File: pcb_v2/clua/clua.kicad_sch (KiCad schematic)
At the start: 168 parts, among them J1 bus_ula_2, J10 bus_rf16_3, J11 UCODE_1, J12 UCODE_2, J13 UCODE_3, J14 UCODE_4, J15 UCODE_5, J16 UCODE_6, J17 UCODE_7, J18 UCODE_INT, J19 9V 1A, J2 bus_ula_1, J20 VOLTMETER, J21 AMPMETER, J3 bus_rf16_1, J4 bus_rf16_2, J5 bus mem 1, J6 bus mem 2, J7 UCODE_0, J8 bus_mgrf_1, J9 bus_mgrf_2, Q1 BC548, Q2 BC548, SW1 RESET, U1 74LS193, U10 MC14495P, U11 IR_HIGH, U12 74LS574, U13 MC14495P, U14 RDADDR_LOW, U15 74LS04, U16 74LS86, U17 RDADDR_HIGH, U18 74LS244, U19 74LS04, U2 74HC238, U20 74LS08, U21 MC14495P, U22 WRADDR_HIGH, U23 WRADDR_LOW, U24 74LS86, U25 74LS125, U26 74LS32, U27 74LS08, U28 74LS74, U29 74LS74, U3 74LS32, U30 74LS138, U31 MC14495P, U32 74HC238, U33 74LS32, U34 LM7805, U4 74LS04, U5 74LS08, U6 74LS157, U7 74LS157, U8 74LS574, U9 IR_LOW

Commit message: .
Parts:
- removed C11: 0.33uF, Capacitor_THT:CP_Radial_D5.0mm_P2.50mm, symbol Device:C_Polarized
- removed C13, C15, C21, C25 (x2), C3, C5: 100nF, Capacitor_THT:C_Disc_D5.1mm_W3.2mm_P5.00mm, symbol Device:C
- removed C14: 0.1uF, Capacitor_THT:CP_Radial_D5.0mm_P2.50mm, symbol Device:C_Polarized
- removed D25, D27, D28, D29, D31: 1N4148, Diode_THT:D_DO-35_SOD27_P7.62mm_Horizontal, symbol Diode:1N4148
- removed D32: 1N4001, Diode_THT:D_DO-41_SOD81_P10.16mm_Horizontal, symbol Diode:1N4001
- removed J10: bus_rf16_3, Connector_PinHeader_2.54mm:PinHeader_2x08_P2.54mm_Vertical, symbol Connector_Generic:Conn_02x08_Odd_Even
- removed J19: 9V 1A, symbol Connector_Generic:Conn_01x02
- removed J20: VOLTMETER, symbol Connector_Generic:Conn_01x02
- removed J21: AMPMETER, symbol Connector_Generic:Conn_01x02
- removed J4: bus_rf16_2, Connector_PinHeader_2.54mm:PinHeader_2x08_P2.54mm_Vertical, symbol Connector_Generic:Conn_02x08_Odd_Even
- removed J5: bus mem 1, Connector_PinHeader_2.54mm:PinHeader_2x08_P2.54mm_Vertical, symbol Connector_Generic:Conn_02x08_Odd_Even
- removed J6: bus mem 2, Connector_PinHeader_2.54mm:PinHeader_2x08_P2.54mm_Vertical, symbol Connector_Generic:Conn_02x08_Odd_Even
- removed J8: bus_mgrf_1, Connector_PinHeader_2.54mm:PinHeader_2x08_P2.54mm_Vertical, symbol Connector_Generic:Conn_02x08_Odd_Even
- removed J9: bus_mgrf_2, Connector_PinHeader_2.54mm:PinHeader_2x08_P2.54mm_Vertical, symbol Connector_Generic:Conn_02x08_Odd_Even
- removed Q1, Q2: BC548, Package_TO_SOT_THT:TO-92_Inline, symbol Transistor_BJT:BC548
- removed R10, R11, R15, R16, R17, R18, R19, R36, R37, R38, R39, R40, R41, R42, R43, R44, R45, R46, R47, R48, R49, R50, R51, R52, R7, R8, R9: 10K, symbol Device:R
- removed R12, R20: 470R, symbol Device:R
- removed R21, R22: 10K, Resistor_THT:R_Axial_DIN0207_L6.3mm_D2.5mm_P7.62mm_Horizontal, symbol Device:R
- removed U13, U21: MC14495P, Package_DIP:DIP-16_W7.62mm, symbol Driver_LED:MC14495P
- removed U14: RDADDR_LOW, 7segdisplay:1-digit-13mm, symbol Display_Character:SA39-11EWA
- removed U15: 74LS04, symbol 74xx:74LS04
- removed U17: RDADDR_HIGH, 7segdisplay:1-digit-13mm, symbol Display_Character:SA39-11EWA
- removed unit 4 of U19
- removed U22: WRADDR_HIGH, 7segdisplay:1-digit-13mm, symbol Display_Character:SA39-11EWA
- removed U23: WRADDR_LOW, 7segdisplay:1-digit-13mm, symbol Display_Character:SA39-11EWA
- removed U3, U33: 74LS32, symbol 74xx:74LS32
- removed U34: LM7805, Package_TO_SOT_THT:TO-220-3_Vertical, symbol Regulator_Linear:LM7805_TO220
- removed unit 7 of U4
- removed unit 5 of U4
- removed unit 2 of U4
- removed unit 1 of U4
- removed unit 3 of U5
- removed unit 5 of U5
- removed unit 2 of U5
- added C24, C25: 100nF, Capacitor_THT:C_Disc_D5.1mm_W3.2mm_P5.00mm, symbol Device:C
- added R2: 10K, symbol Device:R
- added unit 3 of U16
- added unit 2 of U16
- added unit 4 of U16
- added unit 6 of U19
- added unit 3 of U19
- added unit 3 of U27
- added U4: 74LS02, symbol 74xx:74LS02
- J1: value bus_ula_2 -> bus clu 1
- J2: value bus_ula_1 -> bus clu 2
- J3: value bus_rf16_1 -> bus clu 3
- renumbered U4 to U19, U27 to U20, U5 to U27
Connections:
- net UC_read_mem_pc is gone; now on net fetch_cycle: D10.2 (A), D11.2 (A), D12.2 (A), D8.2 (A), D9.2 (A)
- net ~{UC_int_cycle} is gone; now on net ~{UC_int_ready}: R24.1
- net ~{UC_rd_addr_src_reg} is gone; now on net ~{UC_read_addr_src_reg}: U12.1 (OE)
- net ~{clock} is gone; now on net CLOCK: U1.5 (UP)
- net +5V: now also J1.1 (Pin_1), J1.2 (Pin_2), U25.10, U25.12, U25.13, U25.9, C24.2, C25.2, R2.2, U16.10, U16.12, U16.4, U16.5, U16.9, U4.14 (VCC); no longer J2.1 (Pin_1), J2.2 (Pin_2), J3.1 (Pin_1), J3.2 (Pin_2)
- net ADDR_{0}: now also J3.2 (Pin_2)
- net ADDR_{1}: now also J3.1 (Pin_1)
- net CARRY_FLAG: now also J3.6 (Pin_6); no longer J2.8 (Pin_8)
- net CLOCK: now also J2.15 (Pin_15), U27.9; no longer J1.4 (Pin_4)
- net DATA_{0}: now also J1.14 (Pin_14); no longer J2.14 (Pin_14), J3.14 (Pin_14)
- net DATA_{1}: now also J1.13 (Pin_13); no longer J2.13 (Pin_13), J3.13 (Pin_13)
- net DATA_{2}: now also J1.11 (Pin_11); no longer J2.11 (Pin_11), J3.11 (Pin_11)
- net DATA_{3}: now also J1.9 (Pin_9); no longer J2.9 (Pin_9), J3.9 (Pin_9)
- net DATA_{4}: now also J1.7 (Pin_7); no longer J2.7 (Pin_7), J3.7 (Pin_7)
- net DATA_{5}: now also J1.5 (Pin_5); no longer J2.5 (Pin_5), J3.5 (Pin_5)
- net DATA_{6}: now also J1.3 (Pin_3); no longer J2.3 (Pin_3), J3.3 (Pin_3)
- net DATA_{7}: now also J1.4 (Pin_4); no longer J2.4 (Pin_4), J3.4 (Pin_4)
- net GND: now also J1.15 (Pin_15), J1.16 (Pin_16), C24.1, C25.1, U4.7 (GND); no longer J2.15 (Pin_15), J2.16 (Pin_16), J3.15 (Pin_15), J3.16 (Pin_16)
- net INT_MASK_FLAG: now also J3.12 (Pin_12); no longer J1.1 (Pin_1)
- net INT_REQUEST: now also J2.2 (Pin_2)
- net NEGATIVE_FLAG: now also J3.10 (Pin_10); no longer J2.12 (Pin_12)
- net OVERFLOW_FLAG: now also J3.8 (Pin_8); no longer J2.10 (Pin_10)
- net RD_ADDR_0: now also J2.8 (Pin_8); no longer J1.8 (Pin_8)
- net RD_ADDR_1: now also J2.10 (Pin_10); no longer J1.10 (Pin_10)
- net RD_ADDR_2: now also J2.12 (Pin_12); no longer J1.12 (Pin_12)
- net RD_ADDR_3: now also J2.14 (Pin_14); no longer J1.14 (Pin_14)
- net RD_ADDR_4: now also J2.16 (Pin_16); no longer J1.16 (Pin_16)
- net RESET: now also U4.12
- net UC_const_boot_addr: now also U19.6
- net UC_read_mem_const: no longer D26.1 (K)
- net ULA_ENABLE: now also J2.4 (Pin_4), U16.11; no longer J1.2 (Pin_2)
- net WRITE_ENABLE: now also J2.6 (Pin_6), U4.10; no longer J1.15 (Pin_15)
- net WR_ADDR_0: now also J2.5 (Pin_5); no longer J1.5 (Pin_5)
- net WR_ADDR_1: now also J2.7 (Pin_7); no longer J1.7 (Pin_7)
- net WR_ADDR_2: now also J2.9 (Pin_9); no longer J1.9 (Pin_9)
- net WR_ADDR_3: now also J2.11 (Pin_11); no longer J1.11 (Pin_11)
- net WR_ADDR_4: now also J2.13 (Pin_13); no longer J1.13 (Pin_13)
- net ZERO_FLAG: now also J3.4 (Pin_4); no longer J2.6 (Pin_6)
- net fetch_cycle: now also U27.10; no longer J11.16 (Pin_16), J12.16 (Pin_16), J13.16 (Pin_16), J14.16 (Pin_16), J15.16 (Pin_16), J16.16 (Pin_16), J17.16 (Pin_16), J18.16 (Pin_16), J7.16 (Pin_16)
- net low_cycle: now also U4.6
- net reset_high_cycle: now also U4.3
- net reset_low_cycle: now also U4.2, U4.5; no longer D26.2 (A), D30.2 (A)
- net ~{UC_break}: now also J3.5 (Pin_5)
- net ~{UC_int_ready}: now also U19.9; no longer U19.13
- net ~{UC_pcia_swap}: now also J2.3 (Pin_3)
- net ~{UC_pclr_swap}: now also J2.1 (Pin_1)
- net ~{UC_read_mem_const}: now also D26.2 (A), R2.1
- net ~{UC_restart_cycle}: now also D23.2 (A), U1.11 (~{LOAD})
- net ~{UC_ula_enable}: now also U16.13
- net ~{UC_write_enable}: now also D30.2 (A), U4.8
- net ~{condition_true}: now also U4.9
- net at U2.9 (Y6): now also U19.13; no longer D23.2 (A)
- net fetch_clock: now reaches U8.11 (Cp)
- net fetch_clock: now also J11.16 (Pin_16), J12.16 (Pin_16), J13.16 (Pin_16), J14.16 (Pin_16), J15.16 (Pin_16), J16.16 (Pin_16), J17.16 (Pin_16), J18.16 (Pin_16), J7.16 (Pin_16), U27.8
- net at U28.11 (C): now also U19.8; no longer U19.12
- net at U25.2: now also U4.4
- net at U19.4: now also U4.11
- net at U28.1 (~{R}): now also U4.13
- net UC_restart_cycle: no longer names the net of D23.1 (K)
- net UC_restart_cycle: now also U19.12
- net UC_write_enable: no longer names the net of D30.1 (K)
- net UC_write_enable: now also D26.1 (K), U19.5, U4.1
- net condition_true: no longer names the net of U28.6 (~{Q})
- no-connect marks 136 -> 120
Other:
- moved on the sheet: C12, C18, D10, D11, D12, D13, D14, D15, D16, D17, D18, D19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

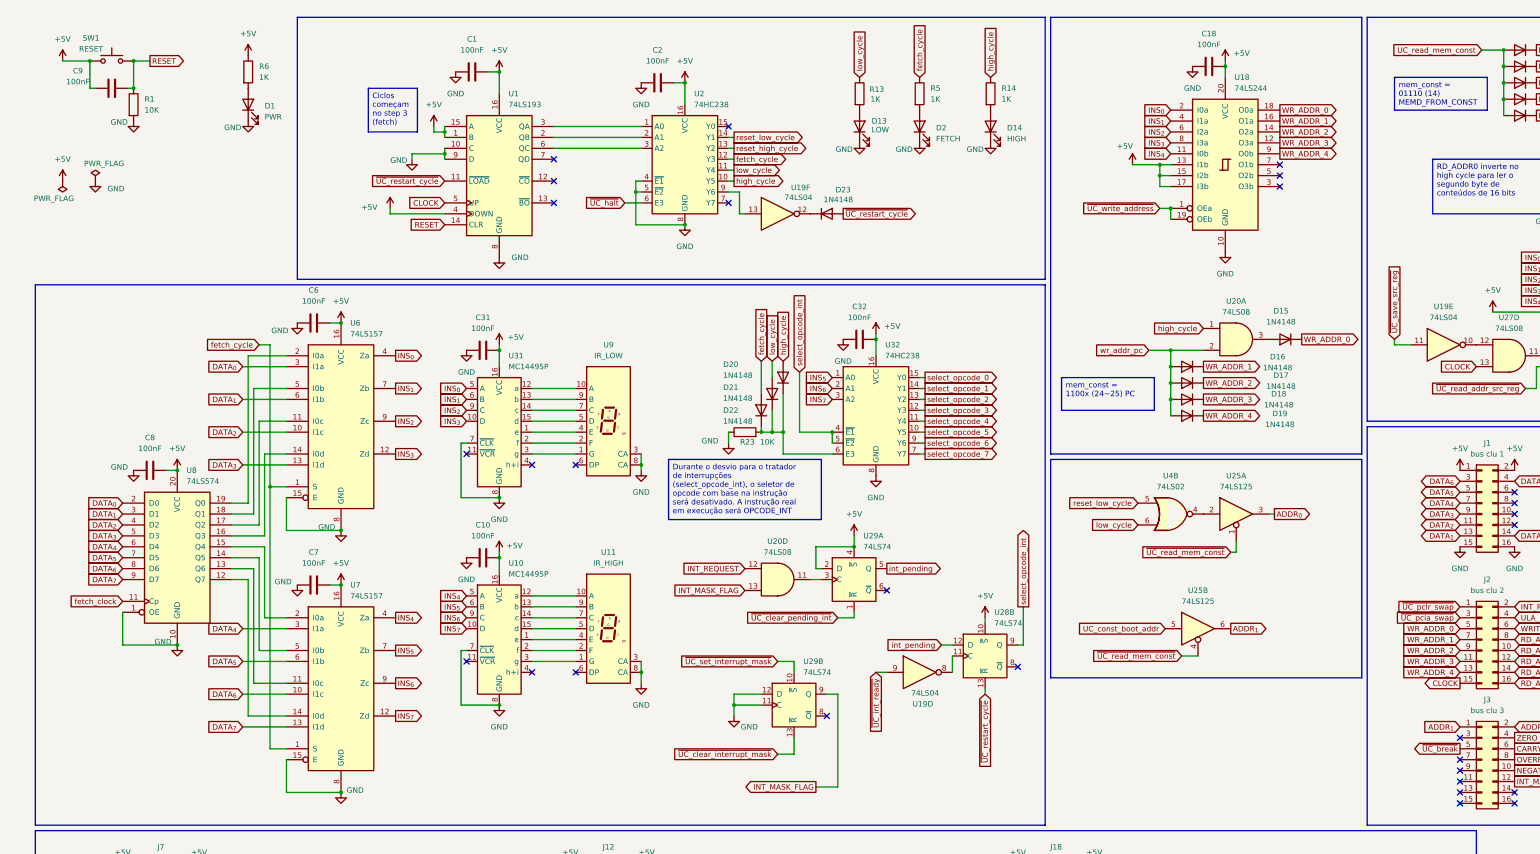
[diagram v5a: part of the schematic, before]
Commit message: movendo itens da clu para o sysbus
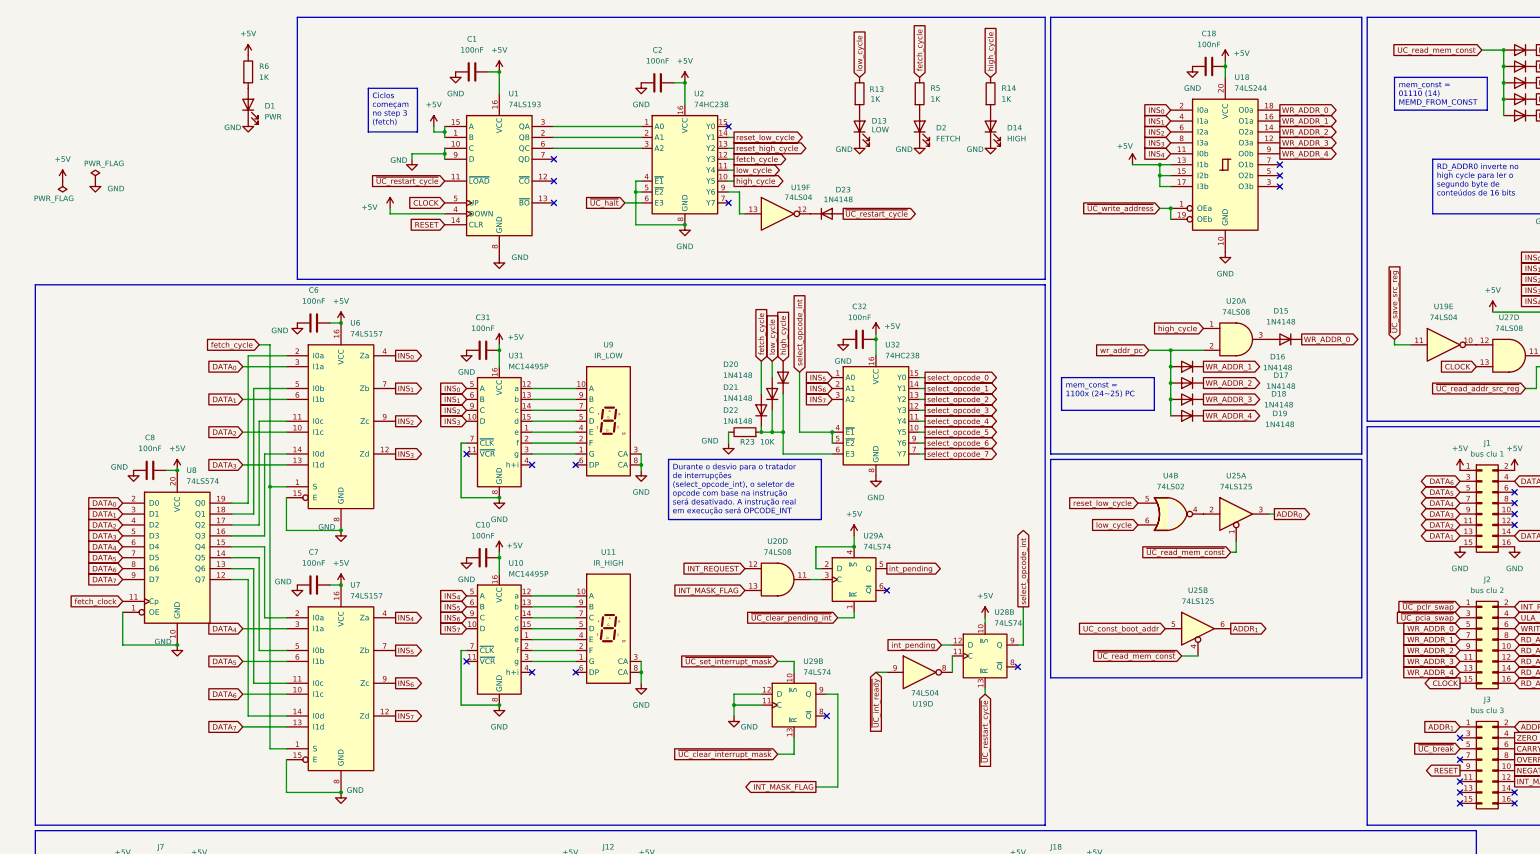
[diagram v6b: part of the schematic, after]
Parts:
- removed C9: 100nF, Capacitor_THT:C_Disc_D4.7mm_W2.5mm_P5.00mm, symbol Device:C
- removed R1: 10K, Resistor_THT:R_Axial_DIN0207_L6.3mm_D2.5mm_P7.62mm_Horizontal, symbol Device:R
- removed SW1: RESET, Button_Switch_THT:SW_PUSH_6mm, symbol Switch:SW_Push
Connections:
- net RESET: now also J3.9 (Pin_9)
- no-connect marks 120 -> 119

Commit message: placa clock gerando os sinais clock e n_clock sincronizados
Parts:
- added D25: IREQ, LED_THT:LED_D5.0mm, symbol Device:LED
- added D27: IPEND, LED_THT:LED_D5.0mm, symbol Device:LED
- added R1 (x2), R3 (x2), R4: 10K, Resistor_THT:R_Axial_DIN0207_L6.3mm_D2.5mm_P7.62mm_Horizontal, symbol Device:R
- added R7, R8: 1K, Resistor_THT:R_Axial_DIN0207_L6.3mm_D2.5mm_P7.62mm_Horizontal, symbol Device:R
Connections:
- net +5V: now also U27.12, U27.13
- net CLOCK: now also J3.15 (Pin_15); no longer J2.15 (Pin_15), U1.5 (UP), U20.5, U27.13, U27.9
- net GND: now also D25.1 (K), D27.1 (K), R1.1, R1.1, R3.1, R3.1, R4.1
- net INT_REQUEST: now also R7.1
- net RD_ADDR_0: no longer D3.1 (K), D8.1 (K)
- net RD_ADDR_1: now also R1.2
- net RD_ADDR_2: now also R3.2
- net RD_ADDR_3: now also R4.2
- net RD_ADDR_4: now also R3.2
- net int_pending: now also R8.1
- net at U12.11 (Cp): now also U19.10; no longer U27.11
- net rd_addr_lsb: now reaches U12.19 (Q0), U16.2
- net rd_addr_lsb: now also D3.1 (K), D8.1 (K), R1.2
- net ~{CLOCK}: now reaches J3.13 (Pin_13)
- net ~{CLOCK}: now also U1.5 (UP), U20.5, U27.9
- new net: D25.2 (A), R7.2
- new net: D27.2 (A), R8.2
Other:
- moved on the sheet: U16A, U19E

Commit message: definindo o layout para empilhar as placas
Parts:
- removed R1, R3: 10K, Resistor_THT:R_Axial_DIN0207_L6.3mm_D2.5mm_P7.62mm_Horizontal, symbol Device:R
- added R10, R9: 10K, Resistor_THT:R_Axial_DIN0207_L6.3mm_D2.5mm_P7.62mm_Horizontal, symbol Device:R
- R2, R23, R24, R25, R26, R27, R28, R29, R30, R31, R32, R33, R35: footprint (none) -> Resistor_THT:R_Axial_DIN0207_L6.3mm_D2.5mm_P7.62mm_Horizontal
- U1, U30, U32, U6, U7, U8: footprint (none) -> Package_DIP:DIP-16_W7.62mm
- U12, U18, U2: footprint (none) -> Package_DIP:DIP-20_W7.62mm
- U16, U19, U20, U24, U25, U26, U27, U28, U29: footprint (none) -> Package_DIP:DIP-14_W10.16mm
- U4: footprint (none) -> Package_DIP:DIP-14_W7.62mm
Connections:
- net GND: now also R10.1, R9.1
- net RD_ADDR_1: now also R9.2
- net RD_ADDR_2: now also R10.2
